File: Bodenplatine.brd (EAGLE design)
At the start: 290 x 145 mm, 118 parts, among them K1 RY612012, K2 RY612012, K3 RY612012, K4 RY612012, K5 RY612012, K6 RY612012, K7 RY612012, K8 RY612012, K9 RY612012, Q1 BC846BLT1SMD, Q2 BC846BLT1SMD, Q3 BC846BLT1SMD, Q4 BC846BLT1SMD, Q5 BC846BLT1SMD, Q6 BC846BLT1SMD, Q7 BC846BLT1SMD, Q8 BC846BLT1SMD, Q9 BC846BLT1SMD, X1 SPRINGCON_AST125_5X2, X10 SPRINGCON_AST125_3X2, X11 SPRINGCON_AST125_4X2, X12 SPRINGCON_AST125_4X2, X13 SPRINGCON_AST125_5X2, X14 236-403, X15 236-402, X2 SPRINGCON_AST125_5X2, X3 SPRINGCON_AST125_5X2, X4 SPRINGCON_AST125_5X2, X5 SPRINGCON_AST125_5X2, X6 SPRINGCON_AST125_5X2, X7 SPRINGCON_AST125_5X2, X8 SPRINGCON_AST125_5X2, X9 SPRINGCON_AST125_5X2

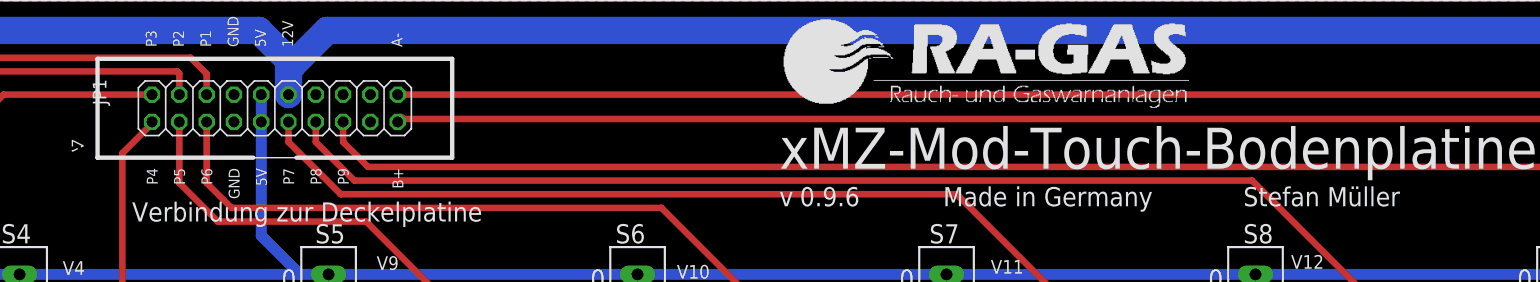
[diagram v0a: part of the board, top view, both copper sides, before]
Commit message: Erste Version der 1.0.0 Produktionsdaten
Versuch alle Datenblätter, eine Kalkulation und Lagerverwaltung und
einer Eagle Datei mit "nur SMD" Bestückungsvariante. Zur Zeit noch nicht
fertig.
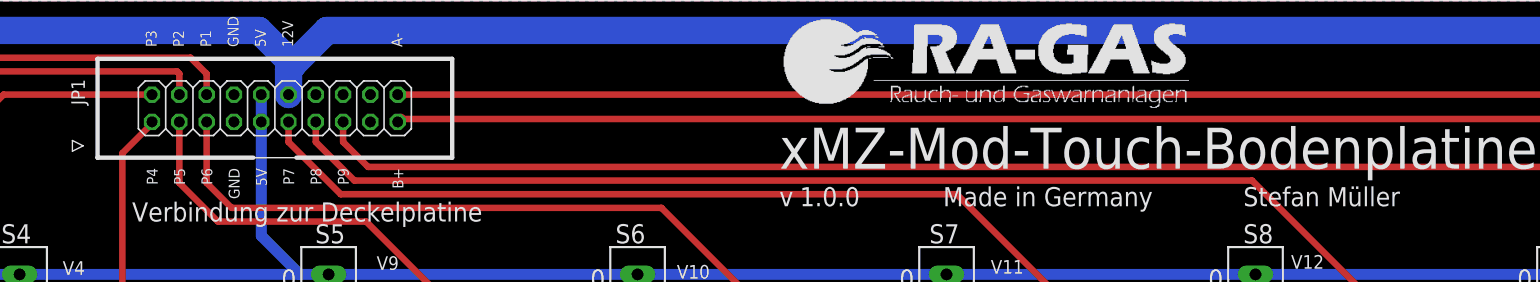
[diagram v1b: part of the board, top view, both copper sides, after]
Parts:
- JP1: device xMZ-Mod-Touch-Bodenplatine:2X10 -> Bodenplatine:2X10
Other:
- board text added: "QtyValue Part Num Package Parts Hersteller Datenblatt 9 1N4148W LL4148-GS08 MINIMELF V5, V6, V7, V8, VVISHAY - LL4148-GS08 - DIODE LL4148_1353494.pdf 9 2k2 MC0063W060352K2 R0603 R5, R6, R7, R8, RMULTICOMP - MC0063W060352K2 R2k2_1788326.pdf 10 3,15AT 3101.0040 FPG4 F1, F2, F3, F4, FSCHURTER - 3101.0040 FUSEHOLDER_PL_FPG_4-40.pdf 1 6,3AT 3101.0040 FPG4 F12 SCHURTER - 3101.0040 FUSEHOLDER_PL_FPG_4-4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"

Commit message: Produktionsdaten exportiert. v1.0.0 soweit fertig
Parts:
- JP1: value Stiftleiste 2x20 pol -> Stiftleiste 2x10 pol; device Bodenplatine:2X10 -> xMZ-Mod-Touch-Bodenplatine:2X10
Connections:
- net 12V: no longer F12.1', F13.1'
- net L: no longer F10.1'
- net N$1: no longer F2.1'
- net N$12: no longer F3.2'
- net N$19: no longer F3.1'
- net N$22: no longer F4.2'
- net N$29: no longer F4.1'
- net N$3: no longer F2.2'
- net N$32: no longer F5.2'
- net N$39: no longer F5.1'
- net N$42: no longer F6.2'
- net N$49: no longer F6.1'
- net N$52: no longer F7.2'
- net N$59: no longer F7.1'
- net N$62: no longer F8.2'
- net N$69: no longer F8.1'
- net N$72: no longer F9.2'
- net N$79: no longer F9.1'
- net N$82: no longer F1.2'
- net N$89: no longer F1.1'
- net N$91: no longer F10.2'
- net N$92: no longer F13.2'
- net N$94: no longer F12.2'
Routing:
- net N$89: track 33.8 -> 28.7 mm
- net N$59: track 34.4 -> 29.3 mm
- net N$19: track 34.4 -> 29.3 mm
- net N$79: track 34.7 -> 29.6 mm
- net N$69: track 34.5 -> 29.4 mm
- net N$49: track 34.4 -> 29.3 mm
- net N$39: track 34.1 -> 29.0 mm
- net N$29: track 34.2 -> 29.1 mm
- net N$1: track 34.2 -> 29.1 mm
- net 12V: track 875.8 -> 880.3 mm
- net N$42: track 13.0 -> 10.2 mm
- net N$82: track 12.5 -> 9.88 mm
- net N$72: track 12.5 -> 9.88 mm
- net N$62: track 12.5 -> 9.88 mm
- net N$52: track 12.5 -> 9.88 mm
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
